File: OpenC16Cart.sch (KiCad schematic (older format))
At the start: 11 parts, among them J1 CONN_01X03, J2 CONN_01X03, J3 CONN_01X03, J4 CONN_01X03, J5 CONN_01X03, J6 CONN_01X03, J7 C16-Exp-Port, U1 27128, U2 27128

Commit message: V2 is almost ready!
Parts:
- removed J1, J4: CONN_01X03, Pin_Headers:Pin_Header_Straight_1x03, symbol CONN_01X03
- removed U1, U2: 27128, pth_circuits:dil_28-600, symbol 27128
- added J1, J4: CONN_02X03, Pin_Headers:Pin_Header_Straight_2x03, symbol CONN_02X03
- added J11, J12, J21, J22: CONN_01X03, Pin_Headers:Pin_Header_Straight_1x03, symbol CONN_01X03
- added U1: 27512 - LO ROM, pth_circuits:dil_28-600_socket, symbol 27512
- added U2: 27512 - HI ROM, pth_circuits:dil_28-600_socket, symbol 27512
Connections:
- net labels added: a14_u1, a14_u2, a15_u1, a15_u2
- wire segments 116 -> 132
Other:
- moved on the sheet: J2, J3, J5, J6

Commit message: Switch to C_0805_HandSoldering and rebuild whatever is needed
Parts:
- C1, C2: footprint smd_cap:c_0805 -> Capacitors_SMD:C_0805_HandSoldering
- J1, J4: footprint Pin_Headers:Pin_Header_Straight_2x03 -> Pin_Headers:Pin_Header_Straight_2x03_Pitch2.54mm
- J11, J12, J2, J21, J22, J3, J5, J6: footprint Pin_Headers:Pin_Header_Straight_1x03 -> Pin_Headers:Pin_Header_Straight_1x03_Pitch2.54mm
- J7: footprint Sukko:C16_Cart_Conn -> C16_Cart_Conn:C16_Cart_Conn
- U1, U2: footprint pth_circuits:dil_28-600_socket -> w_pth_circuits:dil_28-600_socket
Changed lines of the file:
@@
 F 0 "J7" H 3500 5100 50  0000 C CNN
 F 1 "C16-Exp-Port" H 3100 2200 50  0000 C CNN
-F 2 "Sukko:C16_Cart_Conn" H 3100 2000 50  0001 C CNN
+F 2 "C16_Cart_Conn:C16_Cart_Conn" H 3100 2000 50  0001 C CNN
 F 3 "DOCUMENTATION" H 3100 1900 50  0001 C CNN
 	1    3100 3650
@@
 F 0 "C1" H 7075 3100 50  0000 L CNN
 F 1 "C" H 7075 2900 50  0001 L CNN
-F 2 "smd_cap:c_0805" H 7088 2850 50  0001 C CNN
+F 2 "Capacitors_SMD:C_0805_HandSoldering" H 7088 2850 50  0001 C CNN
 F 3 "" H 7050 3000 50  0000 C CNN
 	1    7050 3000
@@
 F 0 "C2" H 9725 3050 50  0000 L CNN
 F 1 "C" H 9725 2850 50  0001 L CNN
-F 2 "smd_cap:c_0805" H 9738 2800 50  0001 C CNN
+F 2 "Capacitors_SMD:C_0805_HandSoldering" H 9738 2800 50  0001 C CNN
 F 3 "" H 9700 2950 50  0000 C CNN
 	1    9700 2950
@@
 F 0 "J2" H 2700 1150 50  0000 C CNN
 F 1 "CONN_01X03" V 2800 950 50  0001 C CNN
-F 2 "Pin_Headers:Pin_Header_Straight_1x03" H 2700 950 50  0001 C CNN
+F 2 "Pin_Headers:Pin_Header_Straight_1x03_Pitch2.54mm" H 2700 950 50  0001 C CNN
 F 3 "" H 2700 950 50  0000 C CNN
 	1    2700 950
@@
 F 0 "J3" H 3850 1150 50  0000 C CNN
 F 1 "CONN_01X03" V 3950 950 50  0001 C CNN
-F 2 "Pin_Headers:Pin_Header_Straight_1x03" H 3850 950 50  0001 C CNN
+F 2 "Pin_Headers:Pin_Header_Straight_1x03_Pitch2.54mm" H 3850 950 50  0001 C CNN
 F 3 "" H 3850 950 50  0000 C CNN
 	1    3850 950
@@
 F 0 "J5" H 7600 1150 50  0000 C CNN
 F 1 "CONN_01X03" V 7700 950 50  0001 C CNN
-F 2 "Pin_Headers:Pin_Header_Straight_1x03" H 7600 950 50  0001 C CNN
+F 2 "Pin_Headers:Pin_Header_Straight_1x03_Pitch2.54mm" H 7600 950 50  0001 C CNN
 F 3 "" H 7600 950 50  0000 C CNN
 	1    7600 950
@@
 F 0 "J6" H 8750 1150 50  0000 C CNN
 F 1 "CONN_01X03" V 8850 950 50  0001 C CNN
-F 2 "Pin_Headers:Pin_Header_Straight_1x03" H 8750 950 50  0001 C CNN
+F 2 "Pin_Headers:Pin_Header_Straight_1x03_Pitch2.54mm" H 8750 950 50  0001 C CNN
 F 3 "" H 8750 950 50  0000 C CNN
 	1    8750 950
@@
 F 0 "U1" H 6700 2550 50  0000 C CNN
 F 1 "27512 - LO ROM" H 6400 4550 50  0000 C CNN
-F 2 "pth_circuits:dil_28-600_socket" H 6400 3550 50  0001 C CNN
+F 2 "w_pth_circuits:dil_28-600_socket" H 6400 3550 50  0001 C CNN
 F 3 "" H 6400 3550 50  0000 C CNN
 	1    6400 3550
@@
 F 0 "U2" H 9350 2550 50  0000 C CNN
 F 1 "27512 - HI ROM" H 9050 4550 50  0000 C CNN
-F 2 "pth_circuits:dil_28-600_socket" H 9050 3550 50  0001 C CNN
+F 2 "w_pth_circuits:dil_28-600_socket" H 9050 3550 50  0001 C CNN
 F 3 "" H 9050 3550 50  0000 C CNN
 	1    9050 3550
@@
 F 0 "J11" H 1800 1750 50  0000 C CNN
 F 1 "CONN_01X03" V 1900 1550 50  0001 C CNN
-F 2 "Pin_Headers:Pin_Header_Straight_1x03" H 1800 1550 50  0001 C CNN
+F 2 "Pin_Headers:Pin_Header_Straight_1x03_Pitch2.54mm" H 1800 1550 50  0001 C CNN
 F 3 "" H 1800 1550 50  0000 C CNN
 	1    1800 1550
@@
 F 0 "J12" H 2950 1750 50  0000 C CNN
 F 1 "CONN_01X03" V 3050 1550 50  0001 C CNN
-F 2 "Pin_Headers:Pin_Header_Straight_1x03" H 2950 1550 50  0001 C CNN
+F 2 "Pin_Headers:Pin_Header_Straight_1x03_Pitch2.54mm" H 2950 1550 50  0001 C CNN
 F 3 "" H 2950 1550 50  0000 C CNN
 	1    2950 1550
@@
 F 0 "J21" H 6700 1750 50  0000 C CNN
 F 1 "CONN_01X03" V 6800 1550 50  0001 C CNN
-F 2 "Pin_Headers:Pin_Header_Straight_1x03" H 6700 1550 50  0001 C CNN
+F 2 "Pin_Headers:Pin_Header_Straight_1x03_Pitch2.54mm" H 6700 1550 50  0001 C CNN
 F 3 "" H 6700 1550 50  0000 C CNN
 	1    6700 1550
@@
 F 0 "J22" H 7850 1750 50  0000 C CNN
 F 1 "CONN_01X03" V 7950 1550 50  0001 C CNN
-F 2 "Pin_Headers:Pin_Header_Straight_1x03" H 7850 1550 50  0001 C CNN
+F 2 "Pin_Headers:Pin_Header_Straight_1x03_Pitch2.54mm" H 7850 1550 50  0001 C CNN
 F 3 "" H 7850 1550 50  0000 C CNN
 	1    7850 1550
@@
 F 0 "J1" H 1500 1150 50  0000 C CNN
 F 1 "CONN_02X03" H 1500 750 50  0000 C CNN
-F 2 "Pin_Headers:Pin_Header_Straight_2x03" H 1500 -250 50  0001 C CNN
+F 2 "Pin_Headers:Pin_Header_Straight_2x03_Pitch2.54mm" H 1500 -250 50  0001 C CNN
 F 3 "" H 1500 -250 50  0000 C CNN
 	1    1500 950
@@
 F 0 "J4" H 6400 1150 50  0000 C CNN
 F 1 "CONN_02X03" H 6400 750 50  0000 C CNN
-F 2 "Pin_Headers:Pin_Header_Straight_2x03" H 6400 -250 50  0001 C CNN
+F 2 "Pin_Headers:Pin_Header_Straight_2x03_Pitch2.54mm" H 6400 -250 50  0001 C CNN
 F 3 "" H 6400 -250 50  0000 C CNN
 	1    6400 950

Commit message: Minor tweaks'n'fixes
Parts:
- J1, J4: footprint Pin_Headers:Pin_Header_Straight_2x03_Pitch2.54mm -> OpenC16Cart:Pin_Header_Straight_2x03-ModSilkS
- J11, J12, J2, J21, J22, J3, J5, J6: footprint Pin_Headers:Pin_Header_Straight_1x03_Pitch2.54mm -> OpenC16Cart:Pin_Header_Straight_1x03-ModSilkS
- J7: footprint C16_Cart_Conn:C16_Cart_Conn -> OpenC16Cart:C16_Cart_Conn
- U1, U2: footprint w_pth_circuits:dil_28-600_socket -> OpenC16Cart:dil_28-600_socket_ThinSilkS
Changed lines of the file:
@@
 Sheet 1 1
 Title "Open Commodore 16/Plus4 Cartridge"
-Date "2017-08-05"
+Date "2018-01-01"
 Rev ""
-Comp ""
+Comp "SukkoPera"
 Comment1 "http://www.zimmers.net/anonftp/pub/cbm/schematics/computers/plus4/Plus_4_Technical_Docs.pdf"
-Comment2 ""
+Comment2 "https://github.com/SukkoPera/OpenC16Cart"
 Comment3 ""
 Comment4 ""
@@
 F 0 "J7" H 3500 5100 50  0000 C CNN
 F 1 "C16-Exp-Port" H 3100 2200 50  0000 C CNN
-F 2 "C16_Cart_Conn:C16_Cart_Conn" H 3100 2000 50  0001 C CNN
+F 2 "OpenC16Cart:C16_Cart_Conn" H 3100 2000 50  0001 C CNN
 F 3 "DOCUMENTATION" H 3100 1900 50  0001 C CNN
 	1    3100 3650
@@
 F 0 "J2" H 2700 1150 50  0000 C CNN
 F 1 "CONN_01X03" V 2800 950 50  0001 C CNN
-F 2 "Pin_Headers:Pin_Header_Straight_1x03_Pitch2.54mm" H 2700 950 50  0001 C CNN
+F 2 "OpenC16Cart:Pin_Header_Straight_1x03-ModSilkS" H 2700 950 50  0001 C CNN
 F 3 "" H 2700 950 50  0000 C CNN
 	1    2700 950
@@
 F 0 "J3" H 3850 1150 50  0000 C CNN
 F 1 "CONN_01X03" V 3950 950 50  0001 C CNN
-F 2 "Pin_Headers:Pin_Header_Straight_1x03_Pitch2.54mm" H 3850 950 50  0001 C CNN
+F 2 "OpenC16Cart:Pin_Header_Straight_1x03-ModSilkS" H 3850 950 50  0001 C CNN
 F 3 "" H 3850 950 50  0000 C CNN
 	1    3850 950
@@
 F 0 "J5" H 7600 1150 50  0000 C CNN
 F 1 "CONN_01X03" V 7700 950 50  0001 C CNN
-F 2 "Pin_Headers:Pin_Header_Straight_1x03_Pitch2.54mm" H 7600 950 50  0001 C CNN
+F 2 "OpenC16Cart:Pin_Header_Straight_1x03-ModSilkS" H 7600 950 50  0001 C CNN
 F 3 "" H 7600 950 50  0000 C CNN
 	1    7600 950
@@
 F 0 "J6" H 8750 1150 50  0000 C CNN
 F 1 "CONN_01X03" V 8850 950 50  0001 C CNN
-F 2 "Pin_Headers:Pin_Header_Straight_1x03_Pitch2.54mm" H 8750 950 50  0001 C CNN
+F 2 "OpenC16Cart:Pin_Header_Straight_1x03-ModSilkS" H 8750 950 50  0001 C CNN
 F 3 "" H 8750 950 50  0000 C CNN
 	1    8750 950
@@
 F 0 "U1" H 6700 2550 50  0000 C CNN
 F 1 "27512 - LO ROM" H 6400 4550 50  0000 C CNN
-F 2 "w_pth_circuits:dil_28-600_socket" H 6400 3550 50  0001 C CNN
+F 2 "OpenC16Cart:dil_28-600_socket_ThinSilkS" H 6400 3550 50  0001 C CNN
 F 3 "" H 6400 3550 50  0000 C CNN
 	1    6400 3550
@@
 F 0 "U2" H 9350 2550 50  0000 C CNN
 F 1 "27512 - HI ROM" H 9050 4550 50  0000 C CNN
-F 2 "w_pth_circuits:dil_28-600_socket" H 9050 3550 50  0001 C CNN
+F 2 "OpenC16Cart:dil_28-600_socket_ThinSilkS" H 9050 3550 50  0001 C CNN
 F 3 "" H 9050 3550 50  0000 C CNN
 	1    9050 3550
@@
 F 0 "J11" H 1800 1750 50  0000 C CNN
 F 1 "CONN_01X03" V 1900 1550 50  0001 C CNN
-F 2 "Pin_Headers:Pin_Header_Straight_1x03_Pitch2.54mm" H 1800 1550 50  0001 C CNN
+F 2 "OpenC16Cart:Pin_Header_Straight_1x03-ModSilkS" H 1800 1550 50  0001 C CNN
 F 3 "" H 1800 1550 50  0000 C CNN
 	1    1800 1550
@@
 F 0 "J12" H 2950 1750 50  0000 C CNN
 F 1 "CONN_01X03" V 3050 1550 50  0001 C CNN
-F 2 "Pin_Headers:Pin_Header_Straight_1x03_Pitch2.54mm" H 2950 1550 50  0001 C CNN
+F 2 "OpenC16Cart:Pin_Header_Straight_1x03-ModSilkS" H 2950 1550 50  0001 C CNN
 F 3 "" H 2950 1550 50  0000 C CNN
 	1    2950 1550
@@
 F 0 "J21" H 6700 1750 50  0000 C CNN
 F 1 "CONN_01X03" V 6800 1550 50  0001 C CNN
-F 2 "Pin_Headers:Pin_Header_Straight_1x03_Pitch2.54mm" H 6700 1550 50  0001 C CNN
+F 2 "OpenC16Cart:Pin_Header_Straight_1x03-ModSilkS" H 6700 1550 50  0001 C CNN
 F 3 "" H 6700 1550 50  0000 C CNN
 	1    6700 1550
@@
 F 0 "J22" H 7850 1750 50  0000 C CNN
 F 1 "CONN_01X03" V 7950 1550 50  0001 C CNN
-F 2 "Pin_Headers:Pin_Header_Straight_1x03_Pitch2.54mm" H 7850 1550 50  0001 C CNN
+F 2 "OpenC16Cart:Pin_Header_Straight_1x03-ModSilkS" H 7850 1550 50  0001 C CNN
 F 3 "" H 7850 1550 50  0000 C CNN
 	1    7850 1550
@@
 F 0 "J1" H 1500 1150 50  0000 C CNN
 F 1 "CONN_02X03" H 1500 750 50  0000 C CNN
-F 2 "Pin_Headers:Pin_Header_Straight_2x03_Pitch2.54mm" H 1500 -250 50  0001 C CNN
+F 2 "OpenC16Cart:Pin_Header_Straight_2x03-ModSilkS" H 1500 -250 50  0001 C CNN
 F 3 "" H 1500 -250 50  0000 C CNN
 	1    1500 950
@@
 F 0 "J4" H 6400 1150 50  0000 C CNN
 F 1 "CONN_02X03" H 6400 750 50  0000 C CNN
-F 2 "Pin_Headers:Pin_Header_Straight_2x03_Pitch2.54mm" H 6400 -250 50  0001 C CNN
+F 2 "OpenC16Cart:Pin_Header_Straight_2x03-ModSilkS" H 6400 -250 50  0001 C CNN
 F 3 "" H 6400 -250 50  0000 C CNN
 	1    6400 950

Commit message: Much better
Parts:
- removed C1, C2: C, Capacitors_SMD:C_0805_HandSoldering, symbol C
- removed J1, J4: CONN_02X03, OpenC16Cart:Pin_Header_Straight_2x03-ModSilkS, symbol CONN_02X03
- removed J11, J12, J2, J21, J22, J3, J5, J6: CONN_01X03, OpenC16Cart:Pin_Header_Straight_1x03-ModSilkS, symbol CONN_01X03
- removed J7: C16-Exp-Port, OpenC16Cart:C16_Cart_Conn, symbol C16-Exp-Port
- removed U1: 27512 - LO ROM, OpenC16Cart:dil_28-600_socket_ThinSilkS, symbol 27512
- removed U2: 27512 - HI ROM, OpenC16Cart:dil_28-600_socket_ThinSilkS, symbol 27512
- added C1, C2: 100n, Capacitor_THT:C_Disc_D7.0mm_W2.5mm_P5.00mm, symbol Device:C
- added CN1: C16-Exp-Port, OpenC16Cart:C16_Cart_Conn, symbol C16-Exp-Port:C16-Exp-Port
- added H1: MountingHole, MountingHole:MountingHole_3.2mm_M3, symbol Mechanical:MountingHole
- added J1, J4: Conn_02x03_Odd_Even, Connector_PinHeader_2.54mm:PinHeader_2x03_P2.54mm_Vertical, symbol Connector_Generic:Conn_02x03_Odd_Even
- added J11, J12, J21, J22: Conn_01x03_Male, Connector_PinHeader_2.54mm:PinHeader_1x03_P2.54mm_Vertical, symbol Connector:Conn_01x03_Male
- added U1: 27512 - LO ROM, Package_DIP:DIP-28_W15.24mm_Socket_LongPads, symbol Memory_EPROM:27C512
- added U2: 27512 - HI ROM, Package_DIP:DIP-28_W15.24mm_Socket_LongPads, symbol Memory_EPROM:27C512
- added V0: LICENSE, OpenC16Cart:cc_by_nc_sa, symbol void:Void
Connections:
- net labels added: a11, ~c1hi, ~c1lo
- net labels removed: /ce_u1, /ce_u2, a11_conn, a11_u1, a11_u2
- wire segments 132 -> 135

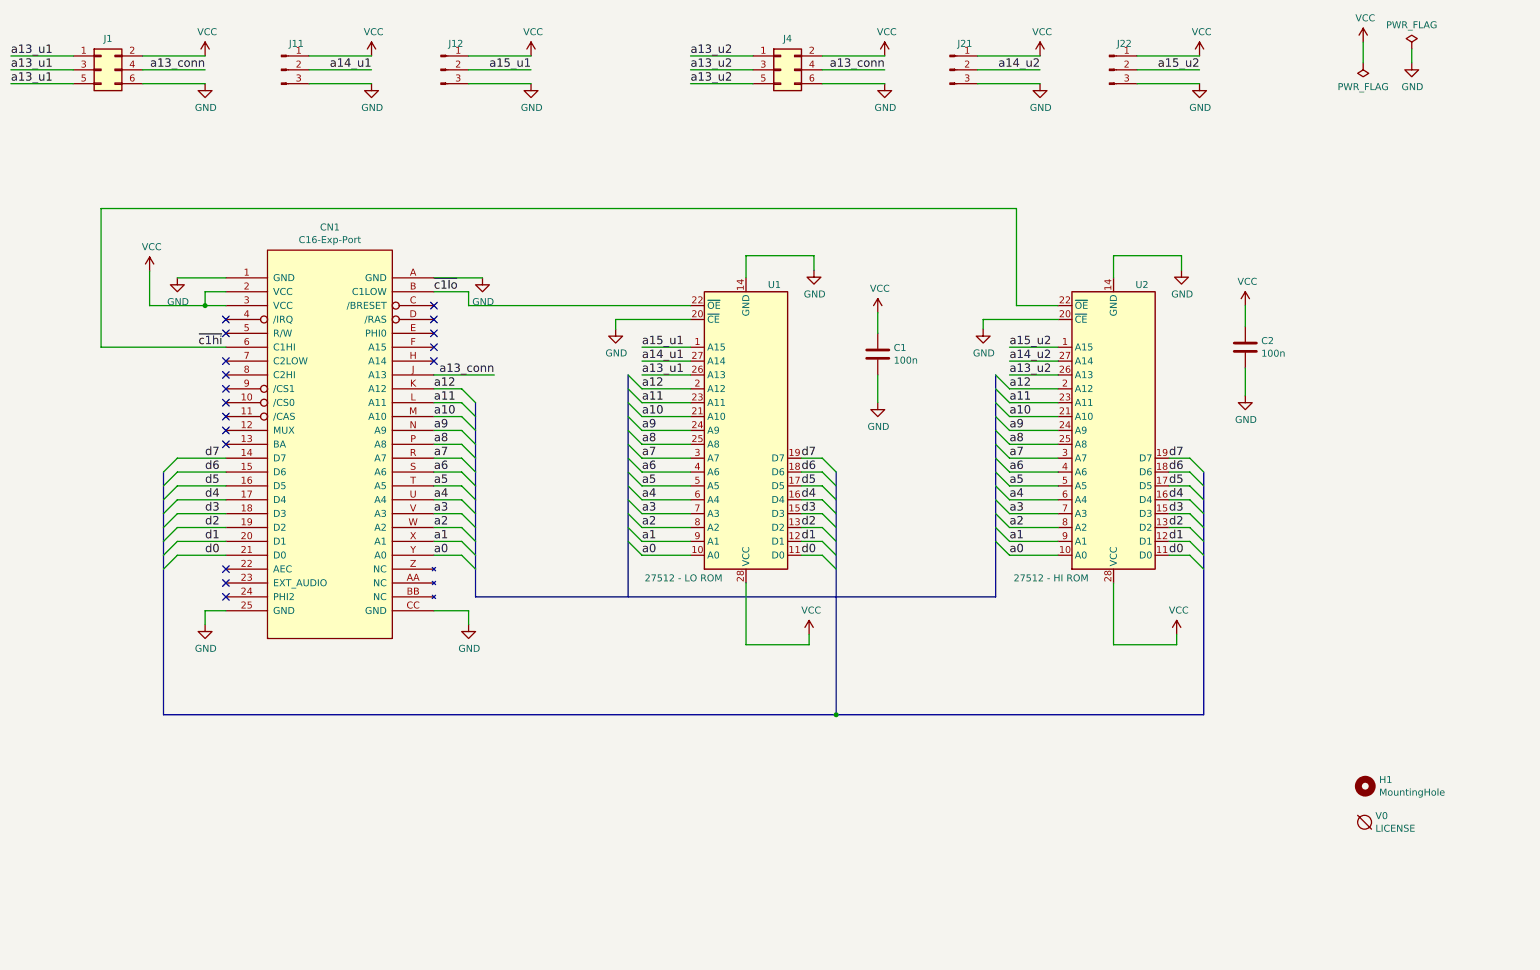
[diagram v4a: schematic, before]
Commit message: Experimental 16/32/64 KB version with 44-pin 2.54" connector
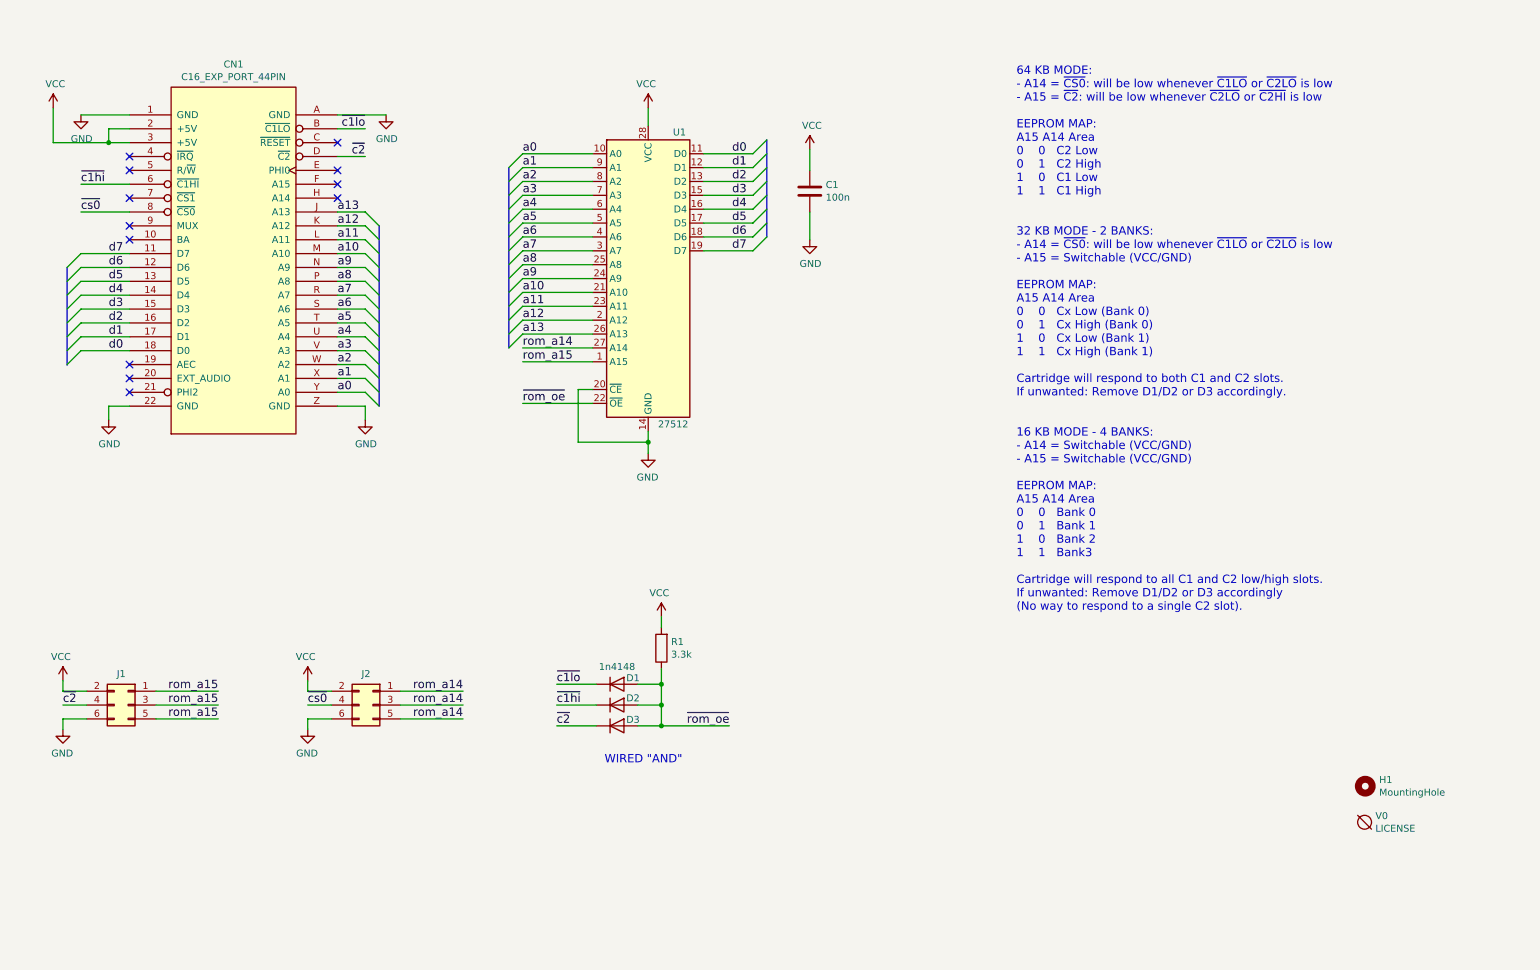
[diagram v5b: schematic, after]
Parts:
- removed C2: 100n, Capacitor_THT:C_Disc_D7.0mm_W2.5mm_P5.00mm, symbol Device:C
- removed CN1: C16-Exp-Port, OpenC16Cart:C16_Cart_Conn, symbol C16-Exp-Port:C16-Exp-Port
- removed J11, J12, J21, J22: Conn_01x03_Male, Connector_PinHeader_2.54mm:PinHeader_1x03_P2.54mm_Vertical, symbol Connector:Conn_01x03_Male
- removed J4: Conn_02x03_Odd_Even, Connector_PinHeader_2.54mm:PinHeader_2x03_P2.54mm_Vertical, symbol Connector_Generic:Conn_02x03_Odd_Even
- removed U2: 27512 - HI ROM, Package_DIP:DIP-28_W15.24mm_Socket_LongPads, symbol Memory_EPROM:27C512
- added CN1: C16_EXP_PORT_44PIN, OpenC16Cart:C16-Exp-Port-44Pin, symbol C16-Exp-Port-44Pin:C16_EXP_PORT_44PIN
- added D1, D2, D3: 1n4148, Diode_THT:D_DO-35_SOD27_P7.62mm_Horizontal, symbol Device:D
- added J2: Conn_02x03_Odd_Even, Connector_PinHeader_2.54mm:PinHeader_2x03_P2.54mm_Vertical, symbol Connector_Generic:Conn_02x03_Odd_Even
- added R1: 3.3k, Resistor_THT:R_Axial_DIN0204_L3.6mm_D1.6mm_P7.62mm_Horizontal, symbol Device:R
- U1: value 27512 - LO ROM -> 27512
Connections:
- net a15_u1 is gone; now on net rom_a15: U1.1 (A15)
- net GND: now also CN1.1 (GND), CN1.22 (GND), CN1.A (GND), CN1.Z (GND), J2.6 (Pin_6)
- net VCC: now also CN1.2 (+5V), CN1.3 (+5V), J2.2 (Pin_2), R1.2
- net a0: now also CN1.Y (A0)
- net a1: now also CN1.X (A1)
- net a10: now also CN1.M (A10)
- net a11: now also CN1.L (A11)
- net a12: now also CN1.K (A12)
- net a2: now also CN1.W (A2)
- net a3: now also CN1.V (A3)
- net a4: now also CN1.U (A4)
- net a5: now also CN1.T (A5)
- net a6: now also CN1.S (A6)
- net a7: now also CN1.R (A7)
- net a8: now also CN1.P (A8)
- net a9: now also CN1.N (A9)
- net d0: now also CN1.18 (D0)
- net d1: now also CN1.17 (D1)
- net d2: now also CN1.16 (D2)
- net d3: now also CN1.15 (D3)
- net d4: now also CN1.14 (D4)
- net d5: now also CN1.13 (D5)
- net d6: now also CN1.12 (D6)
- net d7: now also CN1.11 (D7)
- net ~c1hi: now also CN1.6 (~C1HI), D2.1 (K)
- net ~c1lo: now also CN1.B (~C1LO), D1.1 (K); no longer U1.22 (~OE)
- net a13_conn renamed ~c2
- net ~c2: now also CN1.D (~C2), D3.1 (K)
- net a13_u1 renamed rom_a15
- net rom_a15: no longer U1.26 (A13)
- net a14_u1 renamed rom_a14
- net rom_a14: now also J2.1 (Pin_1), J2.3 (Pin_3), J2.5 (Pin_5)
- new net a13: CN1.J (A13), U1.26 (A13)
- new net ~cs0: CN1.8 (~CS0), J2.4 (Pin_4)
- new net ~rom_oe: D1.2 (A), D2.2 (A), D3.2 (A), R1.1, U1.22 (~OE)
- no-connect marks 17 -> 12
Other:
- note added: "64 KB MODE:\n- A14 = ~CS0~: will be low whenever ~C1LO~ or ~C2LO~ is low\n- A15 = ~C2~: will be low whenever ~C2LO~ or ~C2HI~ is low\n\nEEPROM MAP:\nA15 A14 Area\n0 0 C2 Low\n0 1 C2 High\n1 0 C1 Low\n1 1 C1 High\n\n\n32 KB MODE - 2 BANKS:\n- A14 = ~CS0~: will be low whenever ~C1LO~ or ~C2LO~ is low\n- A15 = Switchable (VCC/GND)\n\nEEPROM MAP:\nA15 A14 Area\n0 0 Cx Low (Bank 0)\n0 1 Cx High (Bank 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"
- note added: "WIRED "AND""
- moved on the sheet: C1, J1, U1

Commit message: Add logo
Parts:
- added V1: LOGO1, OpenC16Cart:logo1, symbol void:Void
- added V2: LOGO2, OpenC16Cart:logo2, symbol void:Void
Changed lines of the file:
@@
 Wire Bus Line
 	4390 1655 4390 2955
+$Comp
+L void:Void V2
+U 1 1 652D5807
+P 9955 6375
+F 0 "V2" H 10033 6421 50  0000 L CNN
+F 1 "LOGO2" H 10033 6330 50  0000 L CNN
+F 2 "OpenC16Cart:logo2" H 9955 6375 50  0001 C CNN
+F 3 "" H 9955 6375 50  0001 C CNN
+	1    9955 6375
+	1    0    0    -1
+$EndComp
+$Comp
+L void:Void V1
+U 1 1 652D5F22
+P 9955 6125
+F 0 "V1" H 10033 6171 50  0000 L CNN
+F 1 "LOGO1" H 10033 6080 50  0000 L CNN
+F 2 "OpenC16Cart:logo1" H 9955 6125 50  0001 C CNN
+F 3 "" H 9955 6125 50  0001 C CNN
+	1    9955 6125
+	1    0    0    -1
+$EndComp
 $EndSCHEMATC
